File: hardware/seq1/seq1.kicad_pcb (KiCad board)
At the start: 2 copper layers, 100 x 100 mm, 85 parts, among them J1 AudioJack2_SwitchT, J2 AudioJack2_SwitchT, J3 Conn_02x08_Odd_Even, J4 AudioJack2_SwitchT, J5 AudioJack2_SwitchT, J6 Conn_02x06_Odd_Even, Q1 2N3904, SW1 SW_Push, SW10 SW_Push, SW11 SW_Push, SW2 SW_Push, SW3 SW_Push, SW4 SW_Push, SW5 SW_Push, SW6 SW_Push, SW7 SW_Push, SW8 SW_Push, SW9 PEC12R-3220F-S0024, U2 74HC4051, U3 74HC4051, U5 128x64 0.96" OLED I2C, U6 TL074, U7 TLV1117-33

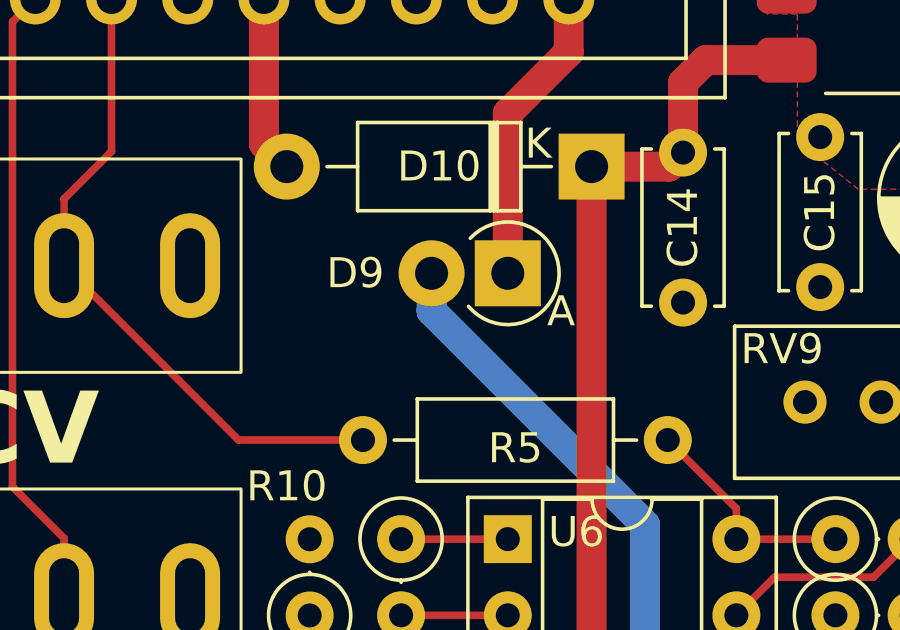
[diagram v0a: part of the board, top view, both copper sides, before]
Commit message: bug in layout: order of pots reversed. Fixes for slide algo in controller, pin definitions and other fixes found in testing
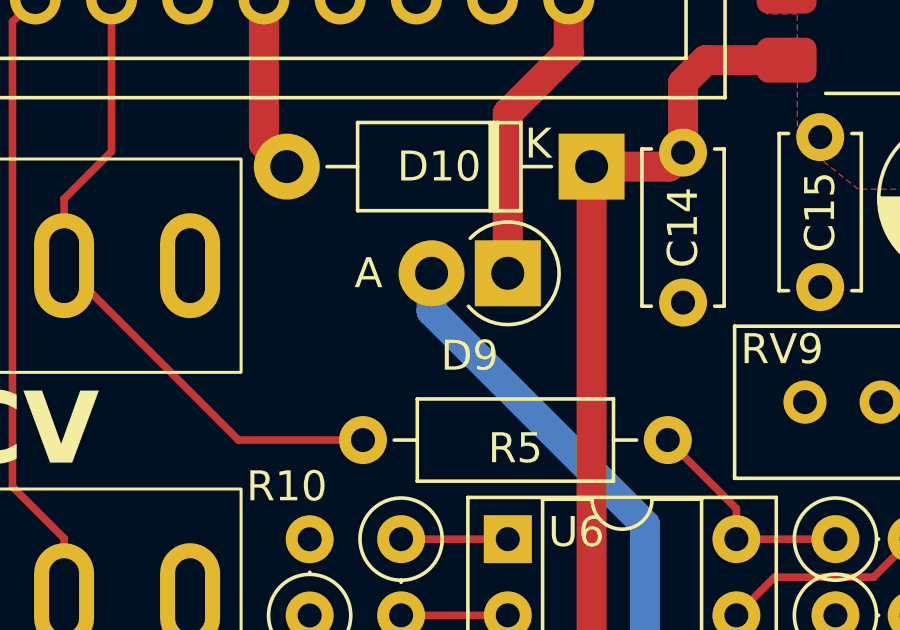
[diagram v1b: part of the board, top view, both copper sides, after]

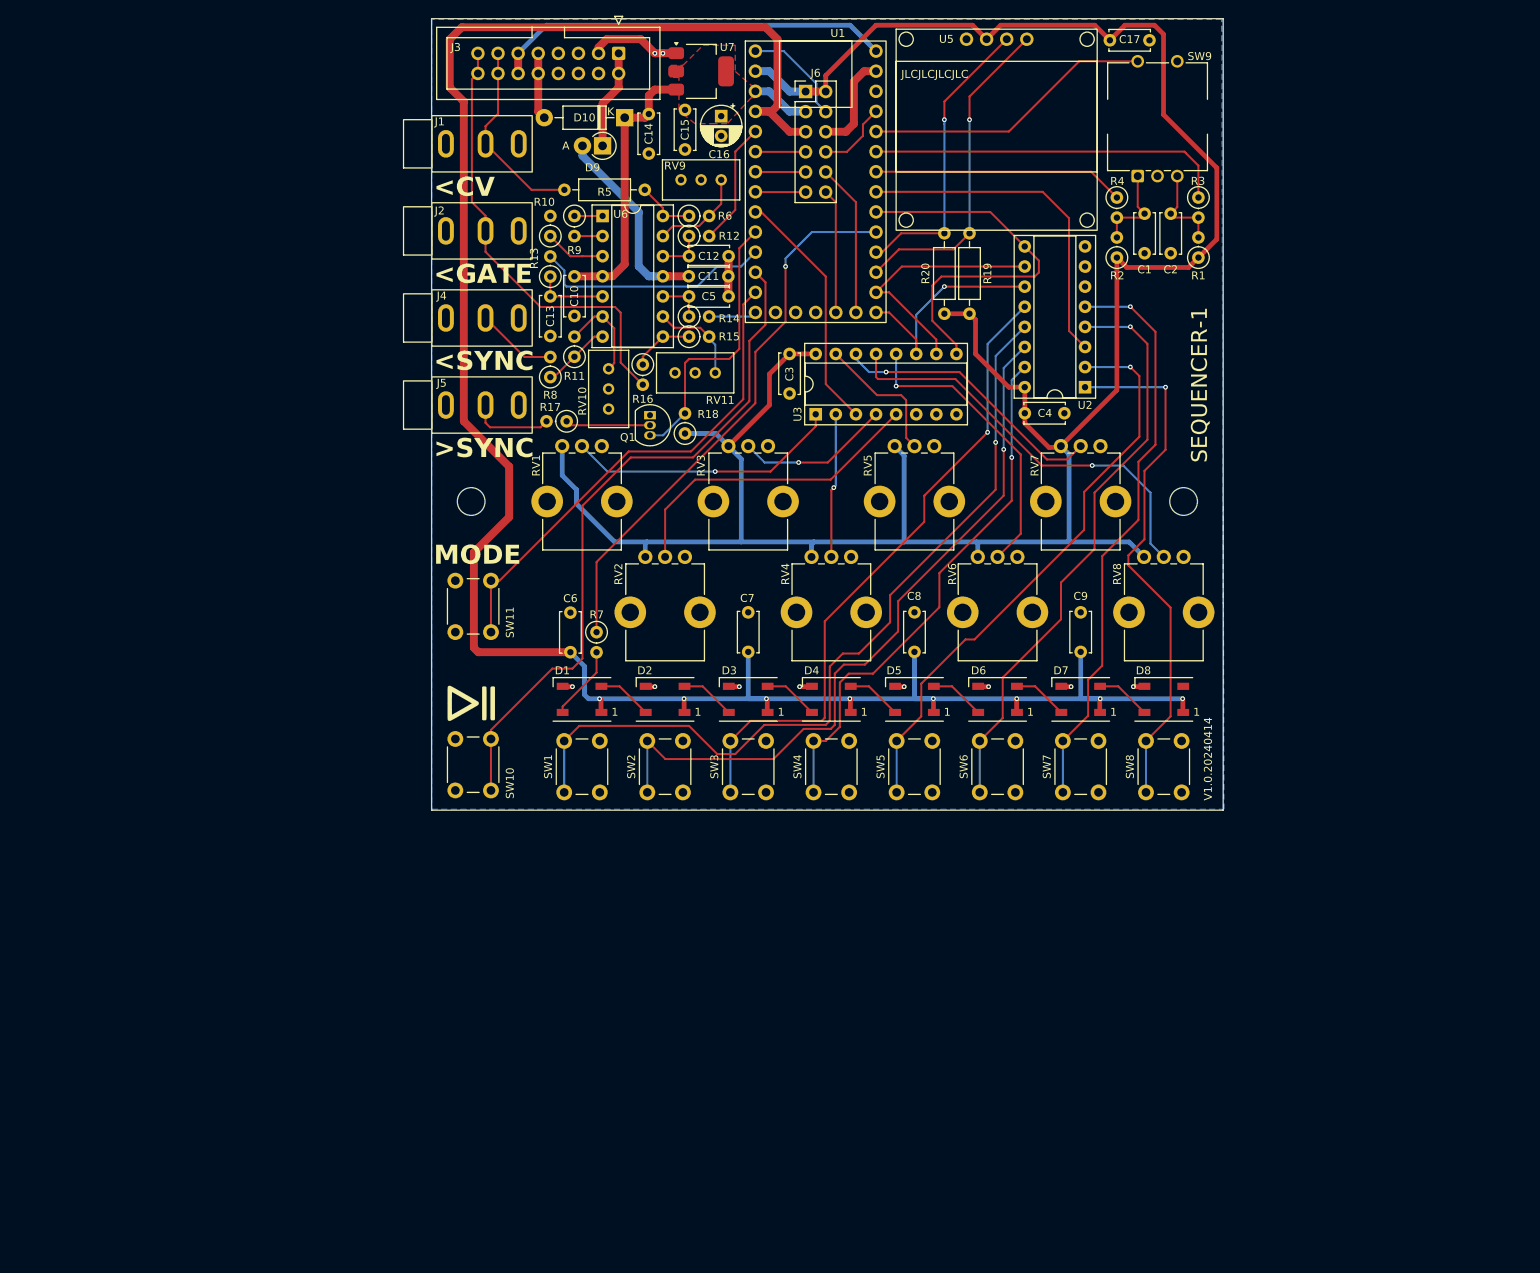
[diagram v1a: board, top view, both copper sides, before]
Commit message: updating the board with new line in
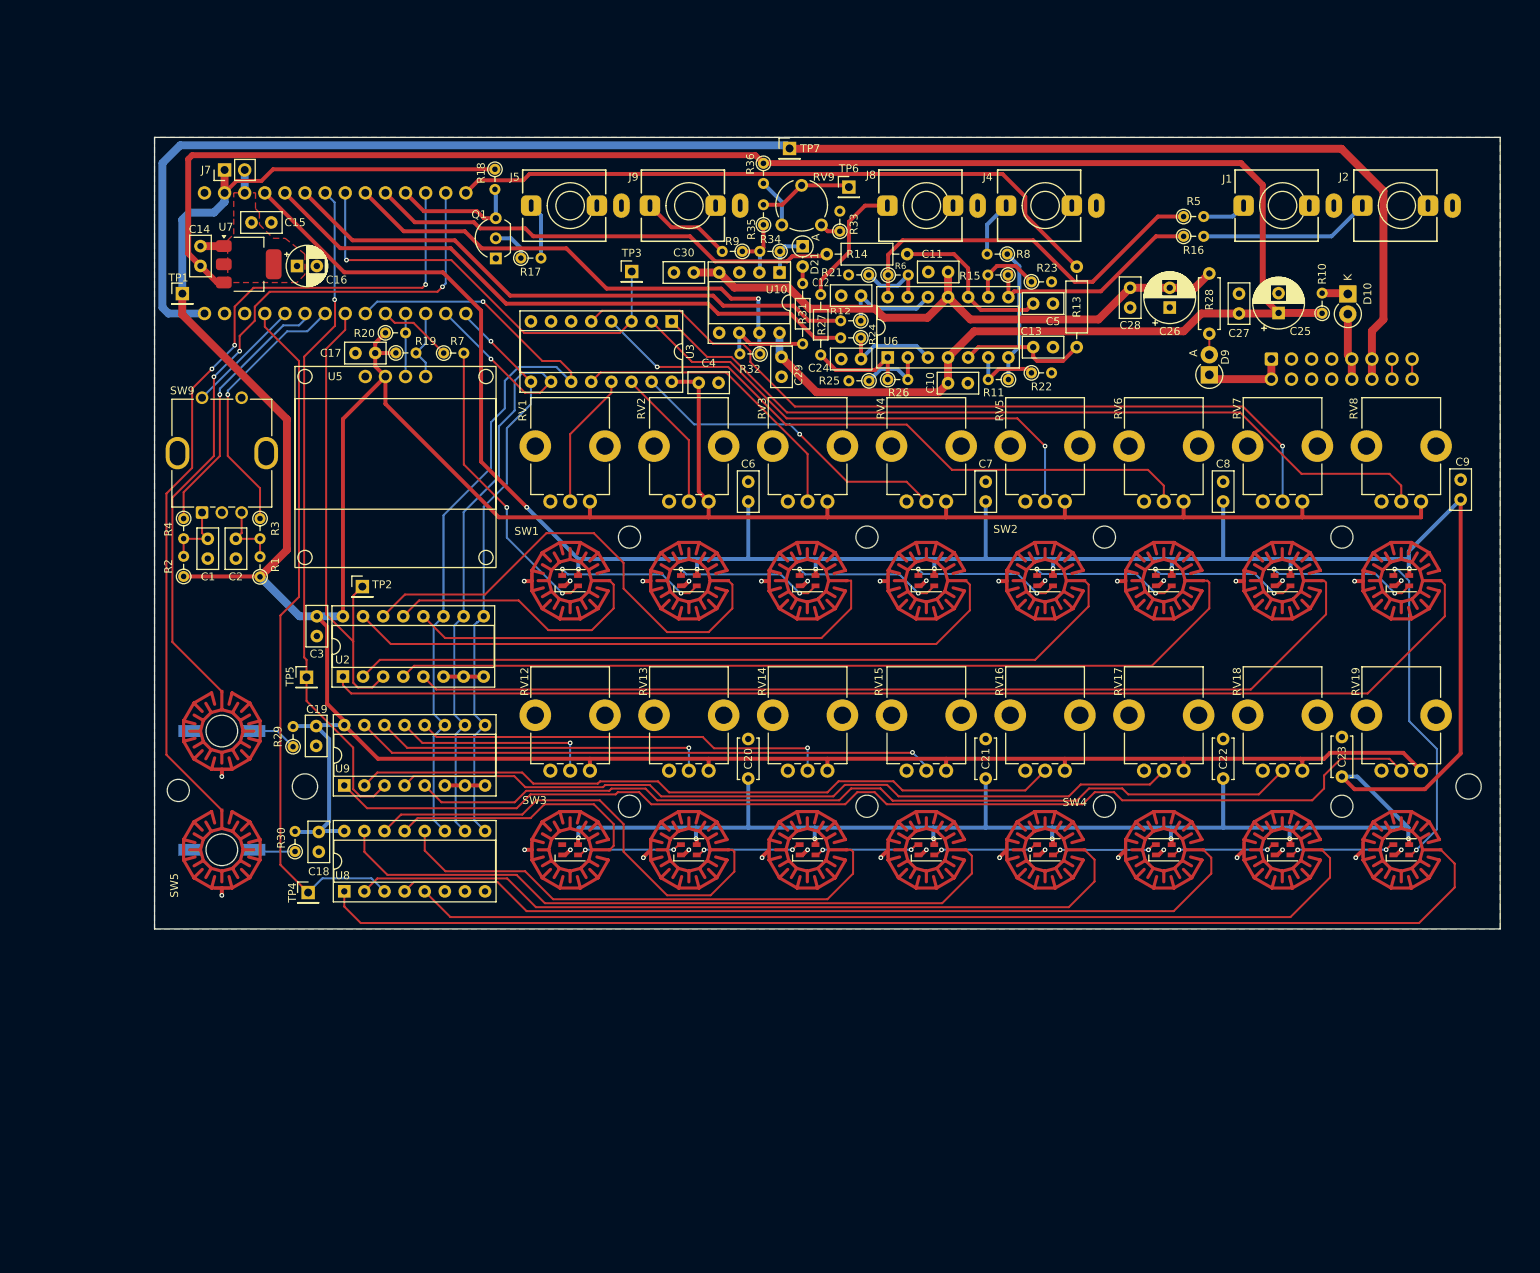
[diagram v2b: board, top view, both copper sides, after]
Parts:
- removed J6: Conn_02x06_Odd_Even, Connector_PinHeader_2.54mm:PinHeader_2x06_P2.54mm_Vertical
- removed RV10, RV11: 50k, Potentiometer_THT:Potentiometer_Bourns_3296W_Vertical
- removed Ref**: Val**, Display_Custom:play_pause_6mm
- removed SW10, SW11, SW6, SW7, SW8: SW_Push, Button_Switch_THT:SW_PUSH_6mm_H5mm
- removed U1: ~, Module_Custom:Adafruit_ItsyBitsy_M0_Express
- added C18: 1u, Capacitor_THT:C_Disc_D5.0mm_W2.5mm_P2.50mm, F.Cu at (65.8, 122.8)
- added C19: 1u, Capacitor_THT:C_Disc_D5.0mm_W2.5mm_P2.50mm, F.Cu at (65.4, 109.4)
- added C20: 1u, Capacitor_THT:C_Disc_D5.0mm_W2.5mm_P5.00mm, F.Cu at (120.0, 116.0)
- added C21: 1u, Capacitor_THT:C_Disc_D5.0mm_W2.5mm_P5.00mm, F.Cu at (150.0, 116.0)
- added C22: 1u, Capacitor_THT:C_Disc_D5.0mm_W2.5mm_P5.00mm, F.Cu at (180.0, 116.0)
- added C23: 1u, Capacitor_THT:C_Disc_D5.0mm_W2.5mm_P5.00mm, F.Cu at (195.0, 115.8)
- added C24: 220p, Capacitor_THT:C_Disc_D5.0mm_W2.5mm_P2.50mm, F.Cu at (131.8, 63.0)
- added C25: 100u, Capacitor_THT:CP_Radial_D6.3mm_P2.50mm, F.Cu at (187.0, 57.2)
- added C26: 100u, Capacitor_THT:CP_Radial_D6.3mm_P2.50mm, F.Cu at (173.2, 56.5)
- added C27: 100n, Capacitor_THT:C_Disc_D5.0mm_W2.5mm_P2.50mm, F.Cu at (182.0, 57.2)
- added C28: 100n, Capacitor_THT:C_Disc_D5.0mm_W2.5mm_P2.50mm, F.Cu at (168.2, 56.5)
- added C29: 100n, Capacitor_THT:C_Disc_D5.0mm_W2.5mm_P2.50mm, F.Cu at (124.2, 62.7)
- added C30: 100n, Capacitor_THT:C_Disc_D5.0mm_W2.5mm_P2.50mm, F.Cu at (110.6, 52.1)
- added D11: SK6805, LED_SMD:LED_SK6805_PLCC4_2.4x2.7mm_P1.3mm, F.Cu at (97.5, 125.0)
- added D12: SK6805, LED_SMD:LED_SK6805_PLCC4_2.4x2.7mm_P1.3mm, F.Cu at (112.5, 125.0)
- added D13: SK6805, LED_SMD:LED_SK6805_PLCC4_2.4x2.7mm_P1.3mm, F.Cu at (127.5, 125.0)
- added D14: SK6805, LED_SMD:LED_SK6805_PLCC4_2.4x2.7mm_P1.3mm, F.Cu at (142.5, 125.0)
- added D15: SK6805, LED_SMD:LED_SK6805_PLCC4_2.4x2.7mm_P1.3mm, F.Cu at (157.5, 125.0)
- added D16: SK6805, LED_SMD:LED_SK6805_PLCC4_2.4x2.7mm_P1.3mm, F.Cu at (172.5, 125.0)
- added D17: SK6805, LED_SMD:LED_SK6805_PLCC4_2.4x2.7mm_P1.3mm, F.Cu at (187.5, 125.0)
- added D18: SK6805, LED_SMD:LED_SK6805_PLCC4_2.4x2.7mm_P1.3mm, F.Cu at (202.5, 125.0)
- added D19: LED, Adafruit_Trellis:LED_3mm_Backside_SMD, F.Cu at (53.5, 110.0)
- added D20: LED, Adafruit_Trellis:LED_3mm_Backside_SMD, F.Cu at (53.5, 125.0)
- added D21: 1N4148, Diode_THT:D_DO-35_SOD27_P2.54mm_Vertical_AnodeUp, F.Cu at (126.9, 48.8)
- added J7: Conn_01x02, Connector_PinHeader_2.54mm:PinHeader_1x02_P2.54mm_Vertical, F.Cu at (53.8, 39.1)
- added J8: AudioJack2_SwitchT, Audio_Jacks:Jack_3.5mm_QingPu_WQP-PJ301M-12_Vertical, F.Cu at (142.5, 43.6)
- added J9: AudioJack2_SwitchT, Audio_Jacks:Jack_3.5mm_QingPu_WQP-PJ301M-12_Vertical, F.Cu at (112.5, 43.6)
- added R21: 33k, Resistor_THT:R_Axial_DIN0204_L3.6mm_D1.6mm_P2.54mm_Vertical, F.Cu at (135.2, 52.4)
- added R22: 33k, Resistor_THT:R_Axial_DIN0204_L3.6mm_D1.6mm_P2.54mm_Vertical, F.Cu at (155.8, 64.8)
- added R23: 33k, Resistor_THT:R_Axial_DIN0204_L3.6mm_D1.6mm_P2.54mm_Vertical, F.Cu at (155.8, 53.2)
- added R24: 10k, Resistor_THT:R_Axial_DIN0204_L3.6mm_D1.6mm_P2.54mm_Vertical, F.Cu at (134.2, 60.3)
- added R25: 33k, Resistor_THT:R_Axial_DIN0204_L3.6mm_D1.6mm_P2.54mm_Vertical, F.Cu at (135.2, 65.8)
- added R26: 18k, Resistor_THT:R_Axial_DIN0204_L3.6mm_D1.6mm_P2.54mm_Vertical, F.Cu at (137.6, 65.6)
- added R27: 1k, Resistor_THT:R_Axial_DIN0204_L3.6mm_D1.6mm_P7.62mm_Horizontal, F.Cu at (129.2, 62.5)
- added R28: 100, Resistor_THT:R_Axial_DIN0207_L6.3mm_D2.5mm_P7.62mm_Horizontal, F.Cu at (178.2, 59.8)
- added R29: 1.2k, Resistor_THT:R_Axial_DIN0204_L3.6mm_D1.6mm_P2.54mm_Vertical, F.Cu at (62.5, 112.0)
- added R30: 1.2k, Resistor_THT:R_Axial_DIN0204_L3.6mm_D1.6mm_P2.54mm_Vertical, F.Cu at (62.8, 125.2)
- added R31: 100k, Resistor_THT:R_Axial_DIN0204_L3.6mm_D1.6mm_P7.62mm_Horizontal, F.Cu at (126.9, 61.1)
- added R32: 33k, Resistor_THT:R_Axial_DIN0204_L3.6mm_D1.6mm_P2.54mm_Vertical, F.Cu at (121.5, 62.4)
- added R33: 22k, Resistor_THT:R_Axial_DIN0204_L3.6mm_D1.6mm_P2.54mm_Vertical, F.Cu at (131.6, 46.9)
- added R34: 100k, Resistor_THT:R_Axial_DIN0204_L3.6mm_D1.6mm_P2.54mm_Vertical, F.Cu at (124.0, 49.4)
- added R35: 100k, Resistor_THT:R_Axial_DIN0204_L3.6mm_D1.6mm_P2.54mm_Vertical, F.Cu at (121.9, 46.1)
- added R36: 22k, Resistor_THT:R_Axial_DIN0204_L3.6mm_D1.6mm_P2.54mm_Vertical, F.Cu at (121.9, 38.3)
- added RV12: 10k, Potentiometer_THT:Potentiometer_Bourns_PTV09A-1_Single_Vertical, F.Cu at (100.0, 115.0)
- added RV13: 10k, Potentiometer_THT:Potentiometer_Bourns_PTV09A-1_Single_Vertical, F.Cu at (115.0, 115.0)
- added RV14: 10k, Potentiometer_THT:Potentiometer_Bourns_PTV09A-1_Single_Vertical, F.Cu at (130.0, 115.0)
- added RV15: 10k, Potentiometer_THT:Potentiometer_Bourns_PTV09A-1_Single_Vertical, F.Cu at (145.0, 115.0)
- added RV16: 10k, Potentiometer_THT:Potentiometer_Bourns_PTV09A-1_Single_Vertical, F.Cu at (160.0, 115.0)
- added RV17: 10k, Potentiometer_THT:Potentiometer_Bourns_PTV09A-1_Single_Vertical, F.Cu at (175.0, 115.0)
- added RV18: 10k, Potentiometer_THT:Potentiometer_Bourns_PTV09A-1_Single_Vertical, F.Cu at (190.0, 115.0)
- added RV19: 10k, Potentiometer_THT:Potentiometer_Bourns_PTV09A-1_Single_Vertical, F.Cu at (205.0, 115.0)
- added TP1: TestPoint, Connector_PinHeader_2.54mm:PinHeader_1x01_P2.54mm_Vertical, F.Cu at (48.5, 54.7)
- added TP2: TestPoint, Connector_PinHeader_2.54mm:PinHeader_1x01_P2.54mm_Vertical, F.Cu at (71.2, 91.8)
- added TP3: TestPoint, Connector_PinHeader_2.54mm:PinHeader_1x01_P2.54mm_Vertical, F.Cu at (105.3, 51.9)
- added TP4: TestPoint, Connector_PinHeader_2.54mm:PinHeader_1x01_P2.54mm_Vertical, F.Cu at (64.4, 130.4)
- added TP5: TestPoint, Connector_PinHeader_2.54mm:PinHeader_1x01_P2.54mm_Vertical, F.Cu at (64.2, 103.2)
- added TP6: TestPoint, Connector_PinHeader_2.54mm:PinHeader_1x01_P2.54mm_Vertical, F.Cu at (132.7, 41.3)
- added TP7: TestPoint, Connector_PinHeader_2.54mm:PinHeader_1x01_P2.54mm_Vertical, F.Cu at (125.2, 36.4)
- added U10: TL072, Package_DIP:DIP-8_W7.62mm_Socket, F.Cu at (124.0, 52.1)
- added U4: ~, Module_Custom:Adafruit_ItsyBitsy_M0_Express_DIP, B.Cu at (67.8, 49.6)
- added U8: 74HC4051, Package_DIP:DIP-16_W7.62mm_Socket, F.Cu at (69.0, 130.2)
- added U9: 74HC4051, Package_DIP:DIP-16_W7.62mm_Socket, F.Cu at (69.0, 116.9)
- C1, C12, C13, C14, C15, C17, C2, C3, C4, C5, C6, C7, C8, C9: footprint Capacitor_THT:C_Disc_D5.0mm_W2.5mm_P5.00mm -> Capacitor_THT:C_Disc_D5.0mm_W2.5mm_P2.50mm
- C10, C11: value 1u -> 100n; footprint Capacitor_THT:C_Disc_D5.0mm_W2.5mm_P5.00mm -> Capacitor_THT:C_Disc_D5.0mm_W2.5mm_P2.50mm
- D1, D2, D3, D4, D5, D6, D7, D8: value WS2812B -> SK6805; footprint LED_SMD:LED_WS2812B_PLCC4_5.0x5.0mm_P3.2mm -> LED_SMD:LED_SK6805_PLCC4_2.4x2.7mm_P1.3mm
- D10: footprint Diode_THT:D_DO-41_SOD81_P10.16mm_Horizontal -> Diode_THT:D_DO-41_SOD81_P2.54mm_Vertical_KathodeUp
- H1, H2: footprint MountingHole:MountingHole_3.5mm -> MountingHole:MountingHole_3.2mm_M3_DIN965
- J1, J2, J4, J5: footprint Connector_Audio_Custom:Mono_Jack_3.5mm_THT_Horizontal -> Audio_Jacks:Jack_3.5mm_QingPu_WQP-PJ301M-12_Vertical
- J3: moved to B.Cu
- Q1: footprint Package_TO_SOT_THT:TO-92_Inline -> Package_TO_SOT_THT:TO-92_Inline_Wide
- R1, R12, R16, R17, R18, R2, R3, R4, R7, R8: footprint Resistor_THT:R_Axial_DIN0207_L6.3mm_D2.5mm_P2.54mm_Vertical -> Resistor_THT:R_Axial_DIN0204_L3.6mm_D1.6mm_P2.54mm_Vertical
- R10: value 10k -> 100; footprint Resistor_THT:R_Axial_DIN0207_L6.3mm_D2.5mm_P2.54mm_Vertical -> Resistor_THT:R_Axial_DIN0204_L3.6mm_D1.6mm_P2.54mm_Vertical
- R11, R15, R6: value 10k -> 18k; footprint Resistor_THT:R_Axial_DIN0207_L6.3mm_D2.5mm_P2.54mm_Vertical -> Resistor_THT:R_Axial_DIN0204_L3.6mm_D1.6mm_P2.54mm_Vertical
- R13, R14: footprint Resistor_THT:R_Axial_DIN0207_L6.3mm_D2.5mm_P2.54mm_Vertical -> Resistor_THT:R_Axial_DIN0207_L6.3mm_D2.5mm_P10.16mm_Horizontal
- R19, R20, R5: footprint Resistor_THT:R_Axial_DIN0207_L6.3mm_D2.5mm_P10.16mm_Horizontal -> Resistor_THT:R_Axial_DIN0204_L3.6mm_D1.6mm_P2.54mm_Vertical
- R9: value 0 -> 100k; footprint Resistor_THT:R_Axial_DIN0207_L6.3mm_D2.5mm_P2.54mm_Vertical -> Resistor_THT:R_Axial_DIN0204_L3.6mm_D1.6mm_P2.54mm_Vertical
- RV9: value 50k -> 10k; footprint Potentiometer_THT:Potentiometer_Bourns_3296W_Vertical -> Potentiometer_THT:Potentiometer_Piher_PT-6-V_Vertical
- SW1, SW2, SW3, SW4: value SW_Push -> SW_Push_x4; footprint Button_Switch_THT:SW_PUSH_6mm_H5mm -> Adafruit_Trellis:SW_Silicone_Keypad_PushButton_10mm_4x1grid_NH
- SW5: value SW_Push -> SW_Push_x2; footprint Button_Switch_THT:SW_PUSH_6mm_H5mm -> Adafruit_Trellis:SW_Silicone_Keypad_PushButton_10mm_2x1grid_NH
- moved SW9 125.6 mm to (51.0, 82.4)
- moved R3 125.3 mm to (58.3, 83.2)
- moved C1 125.3 mm to (51.7, 85.7)
- moved R1 125.2 mm to (58.3, 90.5)
- moved C2 125.0 mm to (55.3, 85.7)
- moved R4 124.7 mm to (48.7, 83.2)
- moved R2 124.6 mm to (48.7, 90.5)
- moved J2 116.2 mm to (202.5, 43.6)
- moved J1 101.4 mm to (187.5, 43.6)
- moved C17 100.9 mm to (72.9, 62.2), turned to 180 degrees
- moved U2 100.6 mm to (68.8, 103.1), turned to 90 degrees
- moved R10 98.0 mm to (192.5, 57.2)
- moved D10 94.0 mm to (195.8, 54.8), turned to -90 degrees
- moved J3 91.1 mm to (186.1, 63.0)
- moved U5 87.1 mm to (75.4, 76.6)
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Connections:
- net Net-(U1-D26/SDA/PA22) renamed /mcu/OLED_SDA
- net Net-(U1-D27/SCL/PA23) renamed /mcu/OLED_SCL
- net SYNC_OUT_O renamed Net-(J4-PadT)
- D1 pad 1: +5V -> Net-(D1-DOUT)
- D1 pad 2: Net-(D1-DOUT) -> GND
- D1 pad 3: GND -> Net-(D1-DIN)
- D1 pad 4: Net-(D1-DIN) -> +5V
- D10 pad 1: +12V -> Net-(D10-K)
- D2 pad 1: +5V -> Net-(D2-DOUT)
- D2 pad 2: Net-(D2-DOUT) -> GND
- D2 pad 3: GND -> Net-(D1-DOUT)
- D2 pad 4: Net-(D1-DOUT) -> +5V
- D3 pad 1: +5V -> Net-(D3-DOUT)
- D3 pad 2: Net-(D3-DOUT) -> GND
- D3 pad 3: GND -> Net-(D2-DOUT)
- D3 pad 4: Net-(D2-DOUT) -> +5V
- D4 pad 1: +5V -> Net-(D4-DOUT)
- D4 pad 2: Net-(D4-DOUT) -> GND
- D4 pad 3: GND -> Net-(D3-DOUT)
- D4 pad 4: Net-(D3-DOUT) -> +5V
- D5 pad 1: +5V -> Net-(D5-DOUT)
- D5 pad 2: Net-(D5-DOUT) -> GND
- D5 pad 3: GND -> Net-(D4-DOUT)
- D5 pad 4: Net-(D4-DOUT) -> +5V
- D6 pad 1: +5V -> Net-(D6-DOUT)
- D6 pad 2: Net-(D6-DOUT) -> GND
- D6 pad 3: GND -> Net-(D5-DOUT)
- D6 pad 4: Net-(D5-DOUT) -> +5V
- D7 pad 1: +5V -> Net-(D7-DOUT)
- D7 pad 2: Net-(D7-DOUT) -> GND
- D7 pad 3: GND -> Net-(D6-DOUT)
- D7 pad 4: Net-(D6-DOUT) -> +5V
- D8 pad 1: +5V -> Net-(D18-DIN)
- D8 pad 2: unconnected-(D8-DOUT-Pad2) -> GND
- D8 pad 3: GND -> Net-(D7-DOUT)
- D8 pad 4: Net-(D7-DOUT) -> +5V
- D9 pad 2: -12V -> Net-(D9-A)
- J1 pad T: CV_O -> Net-(J1-PadT)
- J2 pad T: GATE_O -> Net-(J2-PadT)
- R10 pad 1: Net-(U6A-+) -> +12V
- R10 pad 2: GND -> Net-(D10-K)
- R12 pad 2: CV -> CV_B
- R13 pad 2: SYNC_OUT -> GATE_A
- R14 pad 2: GATE -> GATE_B
- R16 pad 2: GATE_O -> Net-(J2-PadT)
- R5 pad 2: CV_O -> Net-(J1-PadT)
- R9 pad 1: Net-(R9-Pad1) -> Net-(U10A--)
- R9 pad 2: Net-(U6A--) -> Net-(J9-PadT)
- RV1 pad 2: Net-(U3-A4) -> Net-(U3-A0)
- RV2 pad 2: Net-(U3-A5) -> Net-(U3-A1)
- RV3 pad 2: Net-(U3-A7) -> Net-(U3-A3)
- RV4 pad 2: Net-(U3-A6) -> Net-(U3-A2)
- RV5 pad 2: Net-(U3-A2) -> Net-(U3-A6)
- RV6 pad 2: Net-(U3-A3) -> Net-(U3-A7)
- RV7 pad 2: Net-(U3-A1) -> Net-(U3-A5)
- RV8 pad 2: Net-(U3-A0) -> Net-(U3-A4)
- RV9 pad 1: Net-(U6D--) -> Net-(R33-Pad1)
- RV9 pad 2: GND -> Net-(R35-Pad2)
- RV9 pad 3: GND -> Net-(R36-Pad2)
- SW2 pad 1: Net-(U2-A1) -> Net-(U2-A6)
- SW3 pad 1: Net-(U2-A3) -> Net-(U8-A0)
- SW4 pad 1: Net-(U2-A2) -> Net-(U8-A6)
- SW5 pad 1: Net-(U2-A6) -> /mcu/N_RUN
- U2 pad 3: SW_MUX -> SW_MUX_A
- U3 pad 3: POT_MUX -> POT_MUX_A
- U6 pad 1: Net-(R9-Pad1) -> Net-(R26-Pad1)
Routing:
- net +3V3: track 308.5 -> 529.2 mm
- net +12V: track 34.8 -> 251.6 mm
- net +5V_IN: track 50.6 -> 205.8 mm
- net Net-(U8-A4): track 0.00 -> 150.4 mm
- net +5V: track 277.5 -> 425.5 mm, vias 8 -> 17
- net Net-(U9-A4): track 0.00 -> 142.3 mm
- net Net-(U8-A5): track 0.00 -> 122.3 mm
- net Net-(U9-A5): track 0.00 -> 114.0 mm
- net Net-(U8-A7): track 0.00 -> 109.3 mm
- net Net-(U8-A6): track 0.00 -> 100.3 mm
- net Net-(U9-A7): track 0.00 -> 100.2 mm
- net Net-(U9-A6): track 0.00 -> 90.0 mm
- net SW_MUX_B: track 0.00 -> 88.4 mm
- net Net-(U8-A2): track 0.00 -> 86.9 mm
- net POT_MUX_B: track 0.00 -> 84.9 mm, vias 0 -> 1
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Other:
- board size 100 x 100 mm -> 170 x 100 mm
- board text added: "v1.1.20241014 CC BY-SA 4.0 idyllm"
- board text removed: "3V3"
- board text removed: "3V3A"
- board text removed: "5V"
- board text removed: "<CV"
- board text removed: "<GATE"
- board text removed: "<SYNC"
- board text removed: ">SYNC"
- board text removed: "A1"
- board text removed: "A2"
- board text removed: "A3"
- board text removed: "D13"
- board text removed: "D3"
- board text removed: "D4"
- board text removed: "GND"
- board text removed: "JLCJLCJLCJLC"
- board text removed: "MODE"
- board text removed: "RST"
- board text removed: "V1.0.20240414"

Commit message: layout for v2 board (WIP) with risers part of same schematic/PBC
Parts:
- added D22: SB160, Diode_THT:D_DO-35_SOD27_P2.54mm_Vertical_AnodeUp, F.Cu at (97.8, 50.4)
- added J10: Conn_01x04, Connector_PinHeader_2.54mm:PinHeader_1x04_P2.54mm_Vertical, F.Cu at (170.1, 99.0)
- added J11: Conn_01x04, Connector_PinHeader_2.54mm:PinHeader_1x04_P2.54mm_Vertical, F.Cu at (99.0, 99.0)
- added J12: Conn_01x04, Connector_PinHeader_2.54mm:PinHeader_1x04_P2.54mm_Vertical, F.Cu at (205.7, 99.0)
- added J13: Conn_01x04, Connector_PinHeader_2.54mm:PinHeader_1x04_P2.54mm_Vertical, F.Cu at (127.1, 133.0)
- added J14: Conn_01x04, Connector_PinHeader_2.54mm:PinHeader_1x04_P2.54mm_Vertical, F.Cu at (162.6, 133.0)
- added J15: Conn_01x04, Connector_PinHeader_2.54mm:PinHeader_1x04_P2.54mm_Vertical, F.Cu at (91.5, 133.0)
- added J16: Conn_01x04, Connector_PinHeader_2.54mm:PinHeader_1x04_P2.54mm_Vertical, F.Cu at (198.2, 133.0)
- added J17: Conn_01x04, Connector_PinHeader_2.54mm:PinHeader_1x04_P2.54mm_Vertical, F.Cu at (49.2, 100.0)
- added J18: Conn_01x04, Connector_PinHeader_2.54mm:PinHeader_1x04_P2.54mm_Vertical, F.Cu at (31.7, 100.0)
- added J19: Conn_01x04, Connector_PinHeader_2.54mm:PinHeader_1x04_P2.54mm_Vertical, F.Cu at (31.7, 133.5)
- added J20: Conn_01x04, Connector_PinHeader_2.54mm:PinHeader_1x04_P2.54mm_Vertical, F.Cu at (49.2, 133.5)
- added J21: Conn_01x04, Connector_PinHeader_2.54mm:PinHeader_1x04_P2.54mm_Vertical, F.Cu at (127.1, 154.5)
- added J22: Conn_01x04, Connector_PinHeader_2.54mm:PinHeader_1x04_P2.54mm_Vertical, F.Cu at (162.6, 154.5)
- added J23: Conn_01x04, Connector_PinHeader_2.54mm:PinHeader_1x04_P2.54mm_Vertical, F.Cu at (91.5, 154.5)
- added J24: Conn_01x04, Connector_PinHeader_2.54mm:PinHeader_1x04_P2.54mm_Vertical, F.Cu at (198.2, 154.5)
- added J25: Conn_01x04, Connector_PinHeader_2.54mm:PinHeader_1x04_P2.54mm_Vertical, F.Cu at (127.1, 174.5)
- added J26: Conn_01x04, Connector_PinHeader_2.54mm:PinHeader_1x04_P2.54mm_Vertical, F.Cu at (162.6, 174.5)
- added J27: Conn_01x04, Connector_PinHeader_2.54mm:PinHeader_1x04_P2.54mm_Vertical, F.Cu at (91.5, 174.5)
- added J28: Conn_01x04, Connector_PinHeader_2.54mm:PinHeader_1x04_P2.54mm_Vertical, F.Cu at (198.2, 174.5)
- added J6: Conn_01x04, Connector_PinHeader_2.54mm:PinHeader_1x04_P2.54mm_Vertical, F.Cu at (134.6, 99.0)
- added R37: 1k, Resistor_THT:R_Axial_DIN0204_L3.6mm_D1.6mm_P2.54mm_Vertical, F.Cu at (103.3, 50.4)
- C6, C7, C8, C9: footprint Capacitor_THT:C_Disc_D5.0mm_W2.5mm_P2.50mm -> Capacitor_THT:C_Disc_D5.0mm_W2.5mm_P5.00mm
- D10: footprint Diode_THT:D_DO-41_SOD81_P2.54mm_Vertical_KathodeUp -> Diode_THT:D_DO-35_SOD27_P2.54mm_Vertical_AnodeUp
- D21: value 1N4148 -> SB160
- D9: footprint Diode_THT:D_DO-41_SOD81_P2.54mm_Vertical_AnodeUp -> Diode_THT:D_DO-35_SOD27_P2.54mm_Vertical_AnodeUp
- R10, R28: value 100 -> 10
- moved D11 112.5 mm to (202.5, 165.5)
- moved D18 112.5 mm to (97.5, 165.5)
- moved D12 85.2 mm to (187.5, 165.5)
- moved D17 85.2 mm to (112.5, 165.5)
- moved C8 76.3 mm to (159.5, 154.5), turned to 180 degrees
- moved C9 75.3 mm to (194.8, 154.5), turned to 180 degrees
- moved C6 75.1 mm to (104.5, 154.5), turned to 0 degrees
- moved SW1 74.5 mm to (120.0, 165.5)
- moved SW2 74.5 mm to (180.0, 165.5)
- moved C7 74.5 mm to (138.0, 154.5), turned to 0 degrees
- moved C22 62.0 mm to (159.5, 174.5), turned to 180 degrees
- moved D13 60.5 mm to (172.5, 165.5)
- moved D16 60.5 mm to (127.5, 165.5)
- moved C20 60.5 mm to (104.5, 174.5), turned to 0 degrees
- moved C21 59.7 mm to (138.0, 174.5), turned to 0 degrees
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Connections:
- C18 pad 1: +3V3 -> GND
- C18 pad 2: GND -> +3V3
- C20 pad 1: +5V -> /neopxls/+5V_SB3
- C20 pad 2: GND -> /neopxls/GND_SB3
- C21 pad 1: +5V -> /neopxls/+5V_SB3
- C21 pad 2: GND -> /neopxls/GND_SB3
- C22 pad 1: +5V -> /neopxls/+5V_SB3
- C22 pad 2: GND -> /neopxls/GND_SB3
- C23 pad 1: +5V -> /neopxls/+5V_SB3
- C23 pad 2: GND -> /neopxls/GND_SB3
- C6 pad 1: +5V -> /neopxls/+5V_SB2
- C6 pad 2: GND -> /neopxls/GND_SB2
- C7 pad 1: +5V -> /neopxls/+5V_SB2
- C7 pad 2: GND -> /neopxls/GND_SB2
- C8 pad 1: +5V -> /neopxls/+5V_SB2
- C8 pad 2: GND -> /neopxls/GND_SB2
- C9 pad 1: +5V -> /neopxls/+5V_SB2
- C9 pad 2: GND -> /neopxls/GND_SB2
- D1 pad 2: GND -> /neopxls/GND_SB2
- D1 pad 3: Net-(D1-DIN) -> /neopxls/DIN_SB2
- D1 pad 4: +5V -> /neopxls/+5V_SB2
- D11 pad 1: unconnected-(D11-DOUT-Pad1) -> Net-(D11-DOUT)
- D11 pad 2: GND -> /neopxls/GND_SB3
- D11 pad 4: +5V -> /neopxls/+5V_SB3
- D12 pad 2: GND -> /neopxls/GND_SB3
- D12 pad 4: +5V -> /neopxls/+5V_SB3
- D13 pad 2: GND -> /neopxls/GND_SB3
- D13 pad 4: +5V -> /neopxls/+5V_SB3
- D14 pad 2: GND -> /neopxls/GND_SB3
- D14 pad 4: +5V -> /neopxls/+5V_SB3
- D15 pad 2: GND -> /neopxls/GND_SB3
- D15 pad 4: +5V -> /neopxls/+5V_SB3
- D16 pad 2: GND -> /neopxls/GND_SB3
- D16 pad 4: +5V -> /neopxls/+5V_SB3
- D17 pad 2: GND -> /neopxls/GND_SB3
- D17 pad 4: +5V -> /neopxls/+5V_SB3
- D18 pad 2: GND -> /neopxls/GND_SB3
- D18 pad 3: Net-(D18-DIN) -> /neopxls/DIN_SB3
- D18 pad 4: +5V -> /neopxls/+5V_SB3
- D19 pad 1: GND -> /mcu/GND_SB1
- D2 pad 2: GND -> /neopxls/GND_SB2
- D2 pad 4: +5V -> /neopxls/+5V_SB2
- D20 pad 1: GND -> /mcu/GND_SB1
- D21 pad 1: Net-(D21-K) -> CV_IN
- D21 pad 2: Net-(D21-A) -> GND
- D3 pad 2: GND -> /neopxls/GND_SB2
- D3 pad 4: +5V -> /neopxls/+5V_SB2
- D4 pad 2: GND -> /neopxls/GND_SB2
- D4 pad 4: +5V -> /neopxls/+5V_SB2
- D5 pad 2: GND -> /neopxls/GND_SB2
- D5 pad 4: +5V -> /neopxls/+5V_SB2
- D6 pad 2: GND -> /neopxls/GND_SB2
- D6 pad 4: +5V -> /neopxls/+5V_SB2
- D7 pad 2: GND -> /neopxls/GND_SB2
- D7 pad 4: +5V -> /neopxls/+5V_SB2
- D8 pad 1: Net-(D18-DIN) -> /neopxls/DOUT_SB2
- D8 pad 2: GND -> /neopxls/GND_SB2
- D8 pad 4: +5V -> /neopxls/+5V_SB2
- R29 pad 2: +3V3 -> /mcu/3V3_SB1
- R30 pad 2: +3V3 -> /mcu/3V3_SB1
- R31 pad 2: Net-(D21-A) -> Net-(R31-Pad2)
- R32 pad 1: CV_IN -> Net-(R32-Pad1)
- R34 pad 1: Net-(D21-K) -> Net-(R31-Pad2)
- R7 pad 2: Net-(D1-DIN) -> /neopxls/DIN_NPXL
- SW1 pad 1: Net-(U2-A0) -> /neopxls/GND_SB3
- SW1 pad 2: GND -> Net-(J25-Pin_1)
- SW1 pad 3: Net-(U2-A1) -> /neopxls/GND_SB3
- SW1 pad 4: GND -> Net-(J25-Pin_2)
- SW1 pad 5: Net-(U2-A3) -> /neopxls/GND_SB3
- SW1 pad 6: GND -> Net-(J25-Pin_3)
- SW1 pad 7: Net-(U2-A2) -> /neopxls/GND_SB3
- SW1 pad 8: GND -> Net-(J25-Pin_4)
- SW2 pad 1: Net-(U2-A6) -> /neopxls/GND_SB3
- SW2 pad 2: GND -> Net-(J26-Pin_1)
- SW2 pad 3: Net-(U2-A7) -> /neopxls/GND_SB3
- SW2 pad 4: GND -> Net-(J26-Pin_2)
- SW2 pad 5: Net-(U2-A5) -> /neopxls/GND_SB3
- SW2 pad 6: GND -> Net-(J26-Pin_3)
- SW2 pad 7: Net-(U2-A4) -> /neopxls/GND_SB3
- SW2 pad 8: GND -> Net-(J26-Pin_4)
- SW3 pad 1: Net-(U8-A0) -> /neopxls/GND_SB2
- SW3 pad 2: GND -> Net-(J21-Pin_1)
- SW3 pad 3: Net-(U8-A1) -> /neopxls/GND_SB2
- SW3 pad 4: GND -> Net-(J21-Pin_2)
- SW3 pad 5: Net-(U8-A3) -> /neopxls/GND_SB2
- SW3 pad 6: GND -> Net-(J21-Pin_3)
- SW3 pad 7: Net-(U8-A2) -> /neopxls/GND_SB2
- SW3 pad 8: GND -> Net-(J21-Pin_4)
- SW4 pad 1: Net-(U8-A6) -> /neopxls/GND_SB2
- SW4 pad 2: GND -> Net-(J22-Pin_1)
- SW4 pad 3: Net-(U8-A7) -> /neopxls/GND_SB2
- SW4 pad 4: GND -> Net-(J22-Pin_2)
- SW4 pad 5: Net-(U8-A5) -> /neopxls/GND_SB2
- SW4 pad 6: GND -> Net-(J22-Pin_3)
- SW4 pad 7: Net-(U8-A4) -> /neopxls/GND_SB2
- SW4 pad 8: GND -> Net-(J22-Pin_4)
- SW5 pad 1: /mcu/N_RUN -> /mcu/N_RUN_SB1
- SW5 pad 2: GND -> /mcu/GND_SB1
- SW5 pad 3: /mcu/N_MODE -> /mcu/N_MODE_SB1
- SW5 pad 4: GND -> /mcu/GND_SB1
- U10 pad 1: Net-(D21-K) -> Net-(R31-Pad2)
- U10 pad 7: CV_IN -> Net-(R32-Pad1)
- U2 pad 1: Net-(U2-A4) -> Net-(J10-Pin_4)
- U2 pad 12: Net-(U2-A3) -> Net-(J6-Pin_3)
- U2 pad 13: Net-(U2-A0) -> Net-(J6-Pin_1)
- U2 pad 14: Net-(U2-A1) -> Net-(J6-Pin_2)
- U2 pad 15: Net-(U2-A2) -> Net-(J6-Pin_4)
- U2 pad 2: Net-(U2-A6) -> Net-(J10-Pin_1)
- U2 pad 4: Net-(U2-A7) -> Net-(J10-Pin_2)
- U2 pad 5: Net-(U2-A5) -> Net-(J10-Pin_3)
- U8 pad 1: Net-(U8-A4) -> Net-(J14-Pin_4)
- U8 pad 12: Net-(U8-A3) -> Net-(J13-Pin_3)
- U8 pad 13: Net-(U8-A0) -> Net-(J13-Pin_1)
- U8 pad 14: Net-(U8-A1) -> Net-(J13-Pin_2)
- U8 pad 15: Net-(U8-A2) -> Net-(J13-Pin_4)
- U8 pad 2: Net-(U8-A6) -> Net-(J14-Pin_1)
- U8 pad 4: Net-(U8-A7) -> Net-(J14-Pin_2)
- U8 pad 5: Net-(U8-A5) -> Net-(J14-Pin_3)
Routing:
- net /neopxls/+5V_SB3: track 0.00 -> 208.2 mm, vias 0 -> 16
- net /neopxls/+5V_SB2: track 0.00 -> 208.2 mm, vias 0 -> 16
- net +5V: track 425.5 -> 241.6 mm, vias 17 -> 1
- net Net-(U8-A4): track 150.4 -> 0.00 mm
- net Net-(U2-A4): track 149.5 -> 0.00 mm
- net /neopxls/DOUT_NPXL_1: track 0.00 -> 143.5 mm
- net Net-(U2-A5): track 123.3 -> 0.00 mm
- net Net-(U8-A5): track 122.3 -> 0.00 mm
- net Net-(J10-Pin_4): track 0.00 -> 112.9 mm
- net Net-(U2-A7): track 109.5 -> 0.00 mm
- net Net-(U8-A7): track 109.3 -> 0.00 mm
- net Net-(J14-Pin_4): track 0.00 -> 104.6 mm, vias 0 -> 1
- net Net-(J10-Pin_1): track 0.00 -> 102.6 mm
- net Net-(U8-A6): track 100.3 -> 0.00 mm
- net Net-(J10-Pin_2): track 0.00 -> 100.2 mm
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- added copper zone on B.Cu, net /mcu/GND_SB1
- added copper zone on B.Cu, net /neopxls/GND_SB2
- added copper zone on B.Cu, net /neopxls/GND_SB3
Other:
- board size 170 x 100 mm -> 190.5 x 141.5 mm
- board text added: "CV A"
- board text added: "CV B"
- board text added: "GATE A"
- board text added: "GATE B"
- board text added: "LINE IN"
- board text added: "SYNC IN"
- board text added: "Split to 1x4, remove from project as separate board"
